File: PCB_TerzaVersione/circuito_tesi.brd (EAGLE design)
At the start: 100 x 80 mm, 55 parts, among them Q1 BSS138, Q2 BSS138, Q3 BSS138, Q4 BSS138

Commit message: Sistemati dettagli
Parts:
- moved LIS3DH 0.41 mm to (43.3, 49.9)
- moved C11 0.30 mm to (26.6, 40.4)
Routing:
- net 1.8V: track 53.0 -> 54.9 mm
- net 3.3V: track 149.6 -> 151.4 mm
- net GND: track 335.1 -> 333.8 mm

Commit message: Sistemati dettagli
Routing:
- net 3.3V: track 151.4 -> 152.2 mm
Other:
- board text added: "ENVIRONMENTAL WEARABLE MONITOR LARES 2022"

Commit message: Prove di thermal vias
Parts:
- moved C1 1.40 mm to (24.6, 49.6)
- moved C2 1.40 mm to (27.2, 47.7)
- moved VR_5 1.40 mm to (24.7, 46.9)
- moved R19 0.45 mm to (29.9, 46.2)
- moved C9 0.40 mm to (29.4, 43.6)
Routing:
- net GND: track 333.8 -> 331.2 mm, vias 6 -> 26
- net VDD: track 33.0 -> 31.6 mm
- net 5V: track 92.9 -> 93.5 mm

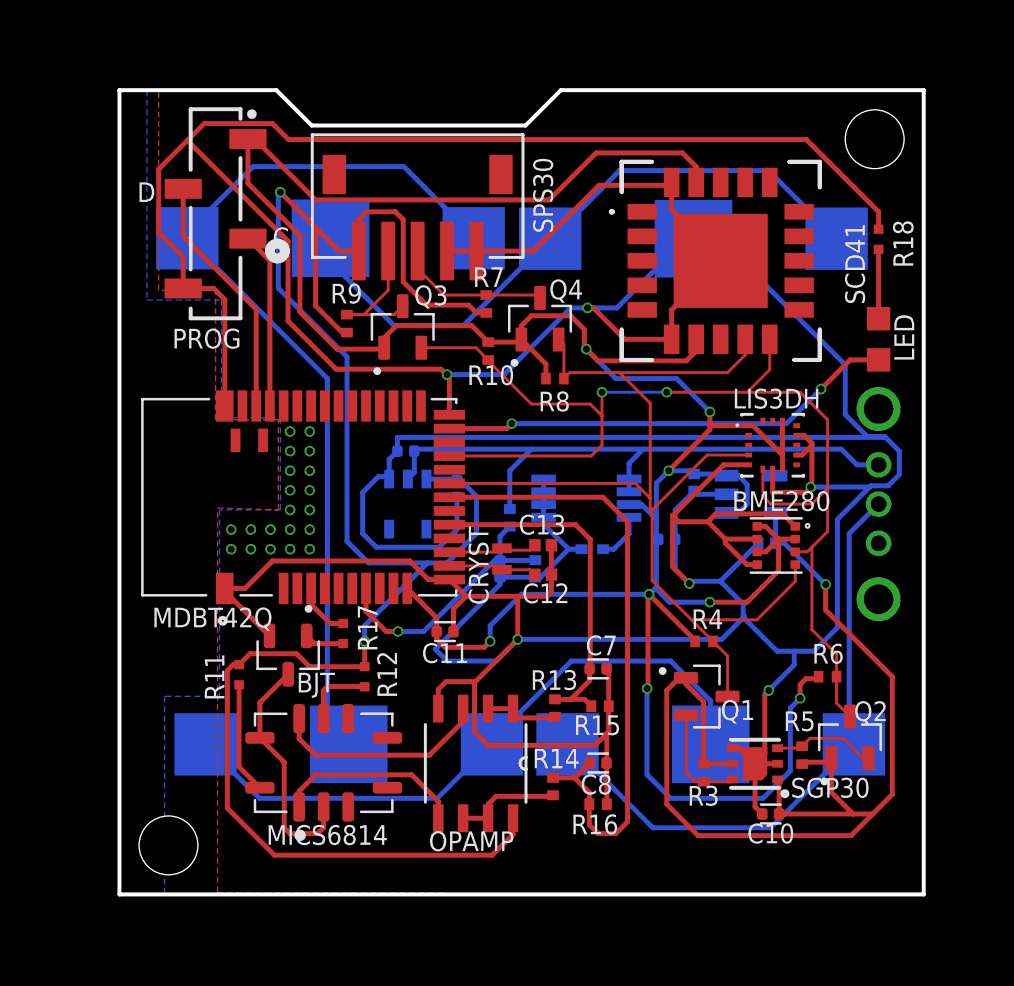
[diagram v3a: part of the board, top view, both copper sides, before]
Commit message: Cambiato layer alle scritte
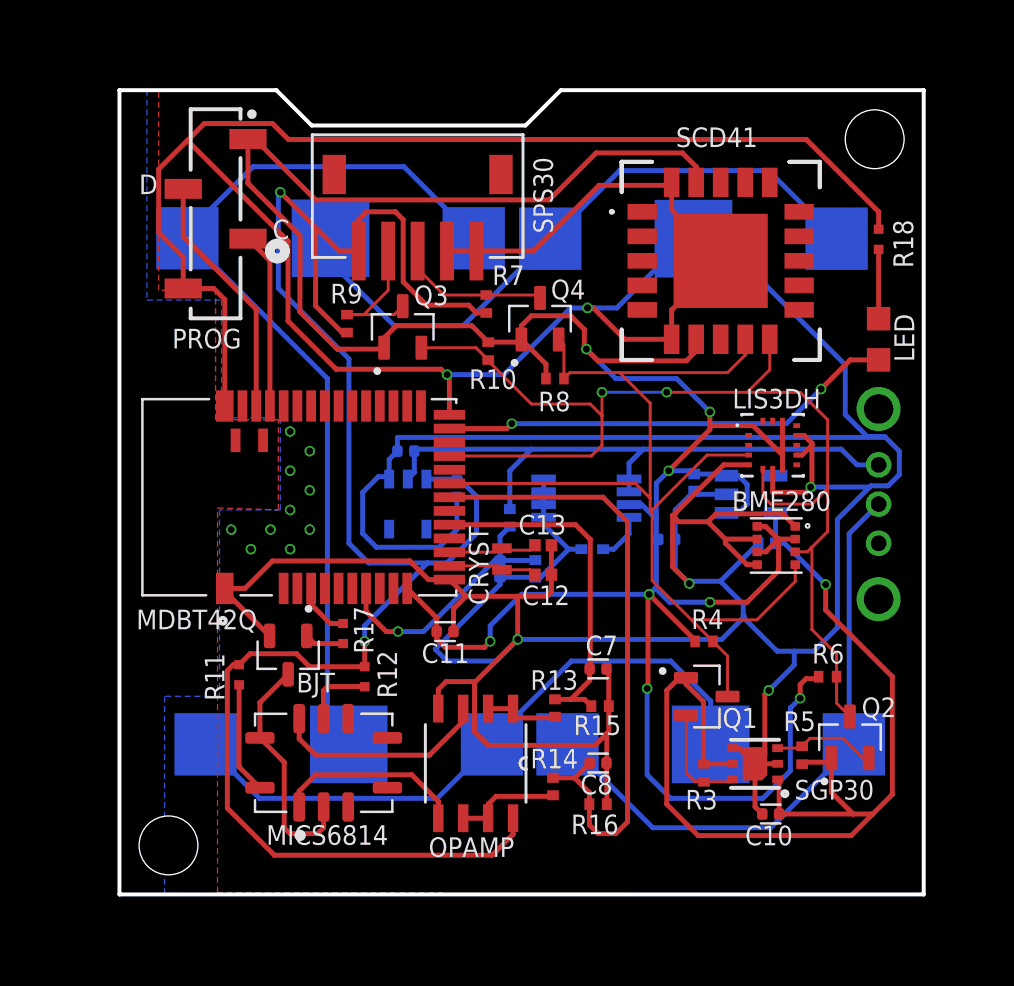
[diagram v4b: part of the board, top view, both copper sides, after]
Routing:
- net GND: vias 26 -> 16

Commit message: Sistemati dettagli
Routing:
- net N$2: track 33.0 -> 37.6 mm
- net GND: track 331.2 -> 330.5 mm
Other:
- board text added: "ENVIRONMENTAL WEARABLE MONITOR"
- board text added: "LARES 2022"
- board text removed: "ENVIRONMENTAL WEARABLE MONITOR LARES 2022"

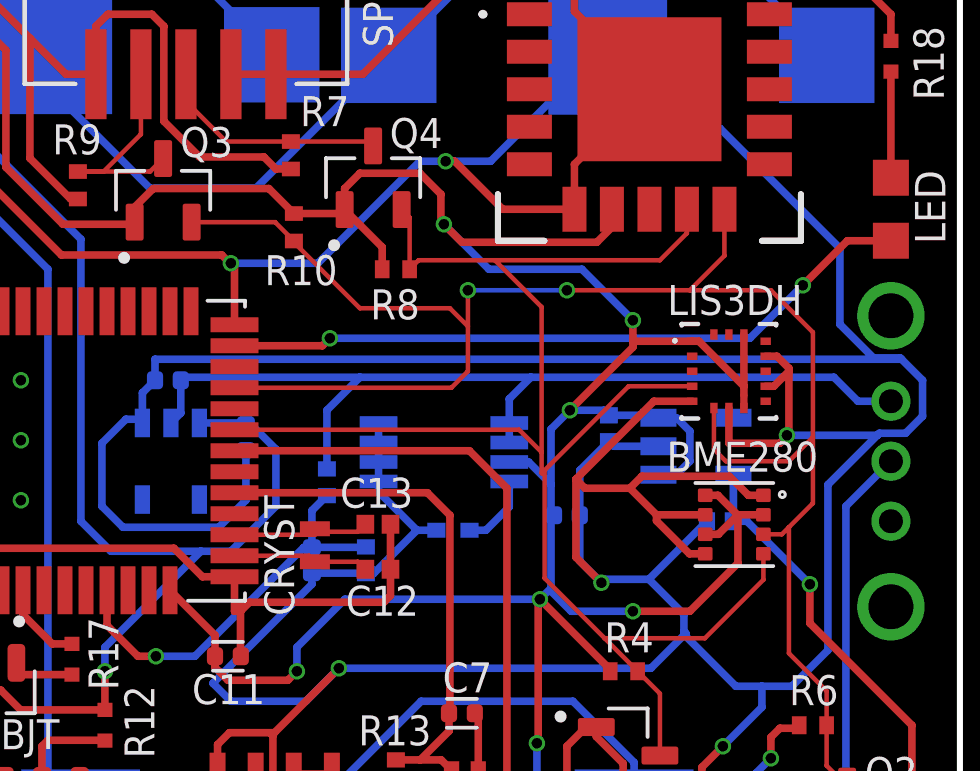
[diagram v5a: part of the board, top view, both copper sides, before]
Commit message: Aggiunti thermal vias
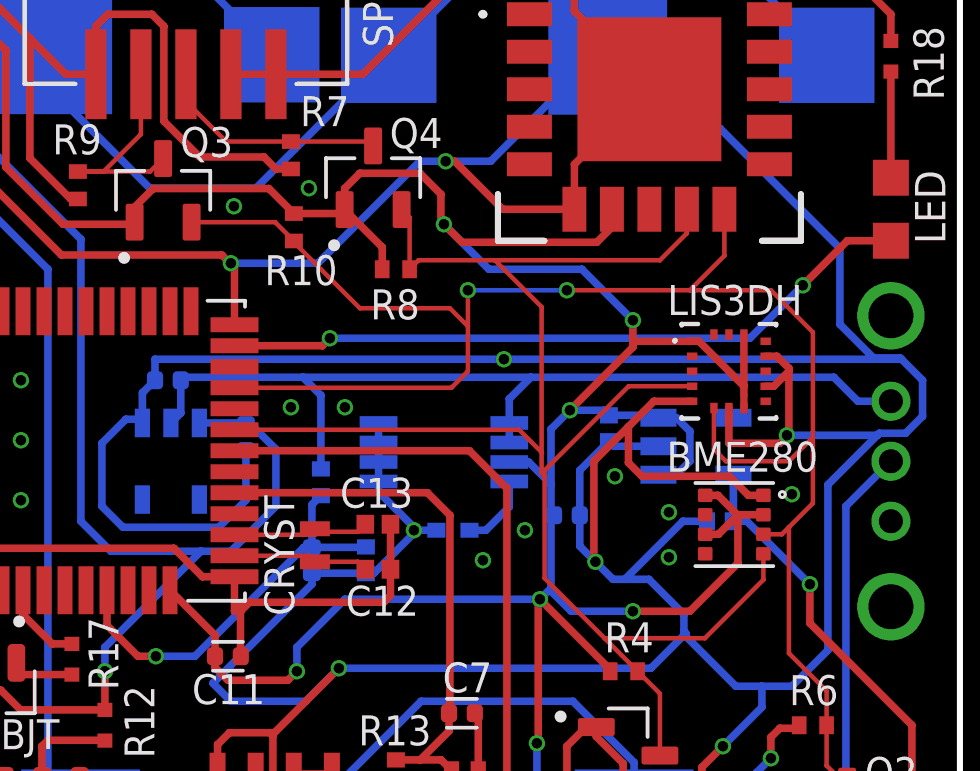
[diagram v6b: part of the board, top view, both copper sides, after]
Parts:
- moved R19 0.20 mm to (29.7, 46.2)
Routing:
- net GND: track 330.5 -> 323.8 mm, vias 16 -> 28
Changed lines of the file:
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@@
 <attribute name="PURCHASE-URL" value="https://pricing.snapeda.com/search/part/ERJ-2GEJ515X/?ref=eda" x="32.1" y="32.5" size="1.778" layer="27" rot="R270" display="off"/>
 </element>
-<element name="R19" library="Res_5,1M_0402" package="RESC1005X40N" value="ERJ-2GEJ515X" x="29.9" y="46.2" smashed="yes" rot="MR270">
-<attribute name="DESCRIPTION" value=" 5.1 MOhms ±5% 0.1W, 1/10W Chip Resistor 0402 (1005 Metric) Automotive AEC-Q200 Thick Film " x="29.9" y="46.2" size="1.778" layer="28" rot="MR270" display="off"/>
-<attribute name="DIGI-KEY_PART_NUMBER" value="P5.1MJTR-ND" x="29.9" y="46.2" size="1.778" layer="28" rot="MR270" display="off"/>
-<attribute name="MF" value="Panasonic" x="29.9" y="46.2" size="1.778" layer="28" rot="MR270" display="off"/>
-<attribute name="MP" value="ERJ-2GEJ515X" x="29.9" y="46.2" size="1.778" layer="28" rot="MR270" display="off"/>
-<attribute name="NAME" x="28.25" y="48.17" size="1" layer="22" rot="MR180"/>
-<attribute name="PACKAGE" value="1005 Panasonic Electronic Components" x="29.9" y="46.2" size="1.778" layer="28" rot="MR270" display="off"/>
-<attribute name="PURCHASE-URL" value="https://pricing.snapeda.com/search/part/ERJ-2GEJ515X/?ref=eda" x="29.9" y="46.2" size="1.778" layer="28" rot="MR270" display="off"/>
+<element name="R19" library="Res_5,1M_0402" package="RESC1005X40N" value="ERJ-2GEJ515X" x="29.7" y="46.2" smashed="yes" rot="MR270">
+<attribute name="DESCRIPTION" value=" 5.1 MOhms ±5% 0.1W, 1/10W Chip Resistor 0402 (1005 Metric) Automotive AEC-Q200 Thick Film " x="29.7" y="46.2" size="1.778" layer="28" rot="MR270" display="off"/>
+<attribute name="DIGI-KEY_PART_NUMBER" value="P5.1MJTR-ND" x="29.7" y="46.2" size="1.778" layer="28" rot="MR270" display="off"/>
+<attribute name="MF" value="Panasonic" x="29.7" y="46.2" size="1.778" layer="28" rot="MR270" display="off"/>
+<attribute name="MP" value="ERJ-2GEJ515X" x="29.7" y="46.2" size="1.778" layer="28" rot="MR270" display="off"/>
+<attribute name="NAME" x="28.05" y="48.17" size="1" layer="22" rot="MR180"/>
+<attribute name="PACKAGE" value="1005 Panasonic Electronic Components" x="29.7" y="46.2" size="1.778" layer="28" rot="MR270" display="off"/>
+<attribute name="PURCHASE-URL" value="https://pricing.snapeda.com/search/part/ERJ-2GEJ515X/?ref=eda" x="29.7" y="46.2" size="1.778" layer="28" rot="MR270" display="off"/>
 </element>
 <element name="R20" library="Res_5,1M_0402" package="RESC1005X40N" value="ERJ-2GEJ515X" x="31.2" y="43.6" smashed="yes" rot="MR90">
@@
 <wire x1="38.15" y1="56.8" x2="40.65" y2="59.3" width="0.254" layer="1"/>
 <via x="45.23500625" y="47.76499375" extent="1-16" drill="0.35"/>
-<via x="39.05" y="42.85" extent="1-16" drill="0.35"/>
+<via x="38.85" y="43.55" extent="1-16" drill="0.35"/>
 <via x="43.1" y="37.4" extent="1-16" drill="0.35"/>
 <wire x1="43.1" y1="37.4" x2="44.4" y2="38.7" width="0.254" layer="16"/>
@@
 <contactref element="C3" pad="2"/>
 <wire x1="41.8" y1="41.23" x2="41.8" y2="41.13" width="0.254" layer="16"/>
-<wire x1="40.633" y1="42.965" x2="39.165" y2="42.965" width="0.254" layer="16"/>
-<wire x1="39.165" y1="42.965" x2="39.05" y2="42.85" width="0.254" layer="16"/>
+<wire x1="40.633" y1="42.965" x2="39.833" y2="42.965" width="0.254" layer="16"/>
+<wire x1="39.833" y1="42.965" x2="39.435" y2="42.965" width="0.254" layer="16"/>
+<wire x1="38.85" y1="43.55" x2="39.435" y2="42.965" width="0.254" layer="16"/>
 <contactref element="C4" pad="1"/>
 <contactref element="C5" pad="1"/>
@@
 <wire x1="38.33" y1="46.598" x2="38.33" y2="45.1" width="0.254" layer="16"/>
 <contactref element="C6" pad="1"/>
-<wire x1="42.568" y1="44.9" x2="40.633" y2="42.965" width="0.254" layer="16"/>
+<wire x1="42.568" y1="44.9" x2="41.768" y2="44.9" width="0.254" layer="16"/>
+<wire x1="41.768" y1="44.9" x2="39.833" y2="42.965" width="0.254" layer="16"/>
 <contactref element="C7" pad="1"/>
 <contactref element="C8" pad="2"/>
@@
 <wire x1="32.02" y1="42.42" x2="31.8" y2="42.2" width="0.254" layer="1"/>
 <wire x1="12" y1="63.97513125" x2="13.462434375" y2="65.437565625" width="0.254" layer="1"/>
-<wire x1="39.05" y1="42.85" x2="38.2" y2="43.7" width="0.254" layer="1"/>
-<wire x1="38.2" y1="46.3" x2="38.2" y2="43.7" width="0.254" layer="1"/>
+<wire x1="38.85" y1="43.55" x2="38.8" y2="43.6" width="0.254" layer="1"/>
+<wire x1="38.8" y1="46.9" x2="38.8" y2="43.6" width="0.254" layer="1"/>
 <wire x1="42.075" y1="48.9" x2="40.8" y2="48.9" width="0.254" layer="1"/>
-<wire x1="40.8" y1="48.9" x2="38.2" y2="46.3" width="0.254" layer="1"/>
+<wire x1="40.8" y1="48.9" x2="39.95" y2="48.05" width="0.254" layer="1"/>
+<wire x1="39.95" y1="48.05" x2="38.8" y2="46.9" width="0.254" layer="1"/>
 <wire x1="45" y1="47.5" x2="43.3" y2="47.5" width="0.254" layer="1"/>
 <wire x1="45.23500625" y1="47.73500625" x2="45.3" y2="47.8" width="0.254" layer="1"/>
@@
 <wire x1="45.23500625" y1="47.76499375" x2="45.23500625" y2="47.73500625" width="0.254" layer="1"/>
 <wire x1="45.23500625" y1="47.73500625" x2="45" y2="47.5" width="0.254" layer="1"/>
-<wire x1="40.4" y1="46.4" x2="40" y2="46" width="0.254" layer="1"/>
-<wire x1="40" y1="46" x2="38.5" y2="46" width="0.254" layer="1"/>
-<wire x1="38.5" y1="46" x2="38.2" y2="46.3" width="0.254" layer="1"/>
 <wire x1="34.83" y1="38.5" x2="34.945" y2="38.385" width="0.254" layer="1"/>
 <wire x1="34.945" y1="38.385" x2="34.945" y2="36.6" width="0.254" layer="1"/>
@@
 <wire x1="43.95" y1="45.765" x2="44.45" y2="45.765" width="0.254" layer="1"/>
 <wire x1="43.95" y1="45.765" x2="43.315" y2="46.4" width="0.254" layer="1"/>
-<wire x1="40.4" y1="46.4" x2="43.315" y2="46.4" width="0.254" layer="1"/>
-<wire x1="40" y1="46" x2="40.885" y2="45.115" width="0.254" layer="1"/>
-<wire x1="40.885" y1="45.115" x2="42.51" y2="45.115" width="0.254" layer="1"/>
-<wire x1="42.51" y1="43.815" x2="41.985" y2="43.815" width="0.254" layer="1"/>
-<wire x1="40.885" y1="44.915" x2="40.885" y2="45.115" width="0.254" layer="1"/>
-<wire x1="41.985" y1="43.815" x2="40.885" y2="44.915" width="0.254" layer="1"/>
+<wire x1="43.315" y1="46.4" x2="40.4" y2="46.4" width="0.254" layer="1"/>
 <wire x1="43.3" y1="48.675" x2="43.3" y2="47.5" width="0.254" layer="1"/>
-<wire x1="38.33" y1="45.1" x2="38.33" y2="43.57" width="0.254" layer="16"/>
-<wire x1="38.33" y1="43.57" x2="39.05" y2="42.85" width="0.254" layer="16"/>
+<wire x1="38.33" y1="45.1" x2="38.33" y2="44.07" width="0.254" layer="16"/>
+<wire x1="38.33" y1="44.07" x2="38.85" y2="43.55" width="0.254" layer="16"/>
 <wire x1="41.8" y1="41.798" x2="40.633" y2="42.965" width="0.254" layer="16"/>
 <wire x1="41.8" y1="41.23" x2="41.8" y2="41.798" width="0.254" layer="16"/>
@@
 <wire x1="42.4" y1="33.66" x2="42.4" y2="36.7" width="0.254" layer="1"/>
 <wire x1="42.4" y1="36.7" x2="43.1" y2="37.4" width="0.254" layer="1"/>
+<via x="45.4" y="45.8" extent="1-16" drill="0.35" diameter="0.3"/>
+<via x="39.5" y="46.4" extent="1-16" drill="0.35" diameter="0.3"/>
+<via x="36.5" y="44.6" extent="1-16" drill="0.35" diameter="0.3"/>
+<via x="35.1" y="43.6" extent="1-16" drill="0.35" diameter="0.3"/>
+<via x="30.5" y="48.7" extent="1-16" drill="0.35" diameter="0.3"/>
+<via x="28.7" y="48.7" extent="1-16" drill="0.35" diameter="0.3"/>
+<via x="35.8" y="50.3" extent="1-16" drill="0.35" diameter="0.3"/>
+<via x="32.8" y="44.6" extent="1-16" drill="0.35" diameter="0.3"/>
+<via x="41.3" y="45.2" extent="1-16" drill="0.35" diameter="0.3"/>
+<via x="26.8" y="55.4" extent="1-16" drill="0.35" diameter="0.3"/>
+<via x="29.3" y="56" extent="1-16" drill="0.35" diameter="0.3"/>
+<via x="41.3" y="43.7" extent="1-16" drill="0.35" diameter="0.3"/>
+<wire x1="40.4" y1="46.4" x2="39.95" y2="46.85" width="0.254" layer="1"/>
+<wire x1="39.95" y1="46.85" x2="39.95" y2="48.05" width="0.254" layer="1"/>
 </signal>
 <signal name="N$11">
@@
 <wire x1="35.978" y1="48.1754" x2="35.978" y2="48.978" width="0.254" layer="16"/>
 <wire x1="35.978" y1="48.978" x2="36.7" y2="49.7" width="0.254" layer="16"/>
-<wire x1="31" y1="49.7" x2="36.7" y2="49.7" width="0.254" layer="16"/>
-<wire x1="29.9" y1="48.6" x2="31" y2="49.7" width="0.254" layer="16"/>
+<wire x1="29.1" y1="49.7" x2="36.7" y2="49.7" width="0.254" layer="16"/>
 <contactref element="R19" pad="1"/>
-<wire x1="29.9" y1="48.6" x2="29.9" y2="46.645" width="0.254" layer="16"/>
+<wire x1="29.7" y1="46.645" x2="29.7" y2="49.1" width="0.254" layer="16"/>
 <contactref element="C1" pad="1"/>
-<wire x1="31" y1="49.7" x2="25.13" y2="49.7" width="0.254" layer="16"/>
+<wire x1="29.1" y1="49.7" x2="25.13" y2="49.7" width="0.254" layer="16"/>
 <wire x1="25.13" y1="49.7" x2="25.03" y2="49.6" width="0.254" layer="16"/>
 <wire x1="25.03" y1="49.6" x2="25.03" y2="48.5063" width="0.254" layer="16"/>
 <wire x1="25.03" y1="48.5063" x2="24.7" y2="48.1763" width="0.254" layer="16"/>
+<wire x1="29.7" y1="49.1" x2="29.1" y2="49.7" width="0.254" layer="16"/>
 </signal>
 <signal name="3.3V">
@@
 <wire x1="25.5" y1="40.4" x2="29.13" y2="44.03" width="0.254" layer="16"/>
 <wire x1="29.4" y1="44.03" x2="31.185" y2="44.03" width="0.254" layer="16"/>
-<wire x1="29.4" y1="44.03" x2="29.4" y2="45.255" width="0.254" layer="16"/>
-<wire x1="29.4" y1="45.255" x2="29.9" y2="45.755" width="0.254" layer="16"/>
+<wire x1="29.4" y1="44.03" x2="29.4" y2="45.455" width="0.254" layer="16"/>
+<wire x1="29.4" y1="45.455" x2="29.7" y2="45.755" width="0.254" layer="16"/>
 </signal>
 <signal name="BJT">
